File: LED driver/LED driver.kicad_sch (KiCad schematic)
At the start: 44 parts, among them J1 Conn_VCC, J2 Conn_LED, J3 Conn_UART, J4 Conn_Boot_Mode, J5 Conn_Aux, Q1 IRFZ44NS, Q2 IRFZ44NS, Q3 IRFZ44NS, Q4 IRFZ44NS, Q5 IRFZ44NS, SW1 SW_Push, U1 ESP32-C3-WROOM-02, U2 MP2359

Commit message: mostly finish led driver
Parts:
- added J1: Conn_VCC_ALT, TerminalBlock_Phoenix:TerminalBlock_Phoenix_MKDS-1,5-2_1x02_P5.00mm_Horizontal, symbol Connector_Generic:Conn_01x02
- D2: footprint Diode_SMD:D_SMB -> Diode_SMD:D_SMA
- J3: renamed from J1; footprint TerminalBlock_Phoenix:TerminalBlock_Phoenix_MKDS-1,5-2_1x02_P5.00mm_Horizontal -> Connector_BarrelJack:BarrelJack_CUI_PJ-063AH_Horizontal
- J6: renamed from J5; now not fitted
- L1: footprint Inductor_SMD:L_Bourns_SRP7028A_7.3x6.6mm -> Inductor_SMD:L_1210_3225Metric_Pad1.42x2.65mm_HandSolder
- Q1, Q2, Q3, Q4, Q5: footprint Package_TO_SOT_SMD:TO-263-2 -> Package_TO_SOT_SMD:SOT-23-3
- SW1: footprint Button_Switch_SMD:SW_Push_1P1T_NO_6x6mm_H9.5mm -> Button_Switch_SMD:SW_SPST_B3U-1000P
- renumbered C5 to C2, C2 to C4, C4 to C5, J3 to J5, R12 to R11, R22 to R12, R11 to R15, R15 to R17, R17 to R18, R18 to R19, R21 to R20
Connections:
- net GND: now also J1.1 (Pin_1)
- net PWM_B: now also R17.2
- net at F1.2, J3.2 (Pin_2): now also J1.2 (Pin_2)
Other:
- moved on the sheet: J3, R17

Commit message: led driver
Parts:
- C1: value .1uF -> 0.1uF
- Q1, Q2, Q3, Q4, Q5: value IRFZ44NS -> ZXMN3A01F; footprint Package_TO_SOT_SMD:SOT-23-3 -> Package_TO_SOT_SMD:SOT-23; symbol Custom:IRFZ44NS -> Transistor_FET:ZXMN3A01F
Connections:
- net B: now also Q2.3 (D); no longer Q2.2 (D)
- net G: now also Q4.3 (D); no longer Q4.2 (D)
- net GND: now also Q1.2 (S), Q2.2 (S), Q3.2 (S), Q4.2 (S), Q5.2 (S); no longer Q1.3 (S), Q2.3 (S), Q3.3 (S), Q4.3 (S), Q5.3 (S)
- net R: now also Q3.3 (D); no longer Q3.2 (D)
- net W: now also Q1.3 (D); no longer Q1.2 (D)
- net WW: now also Q5.3 (D); no longer Q5.2 (D)

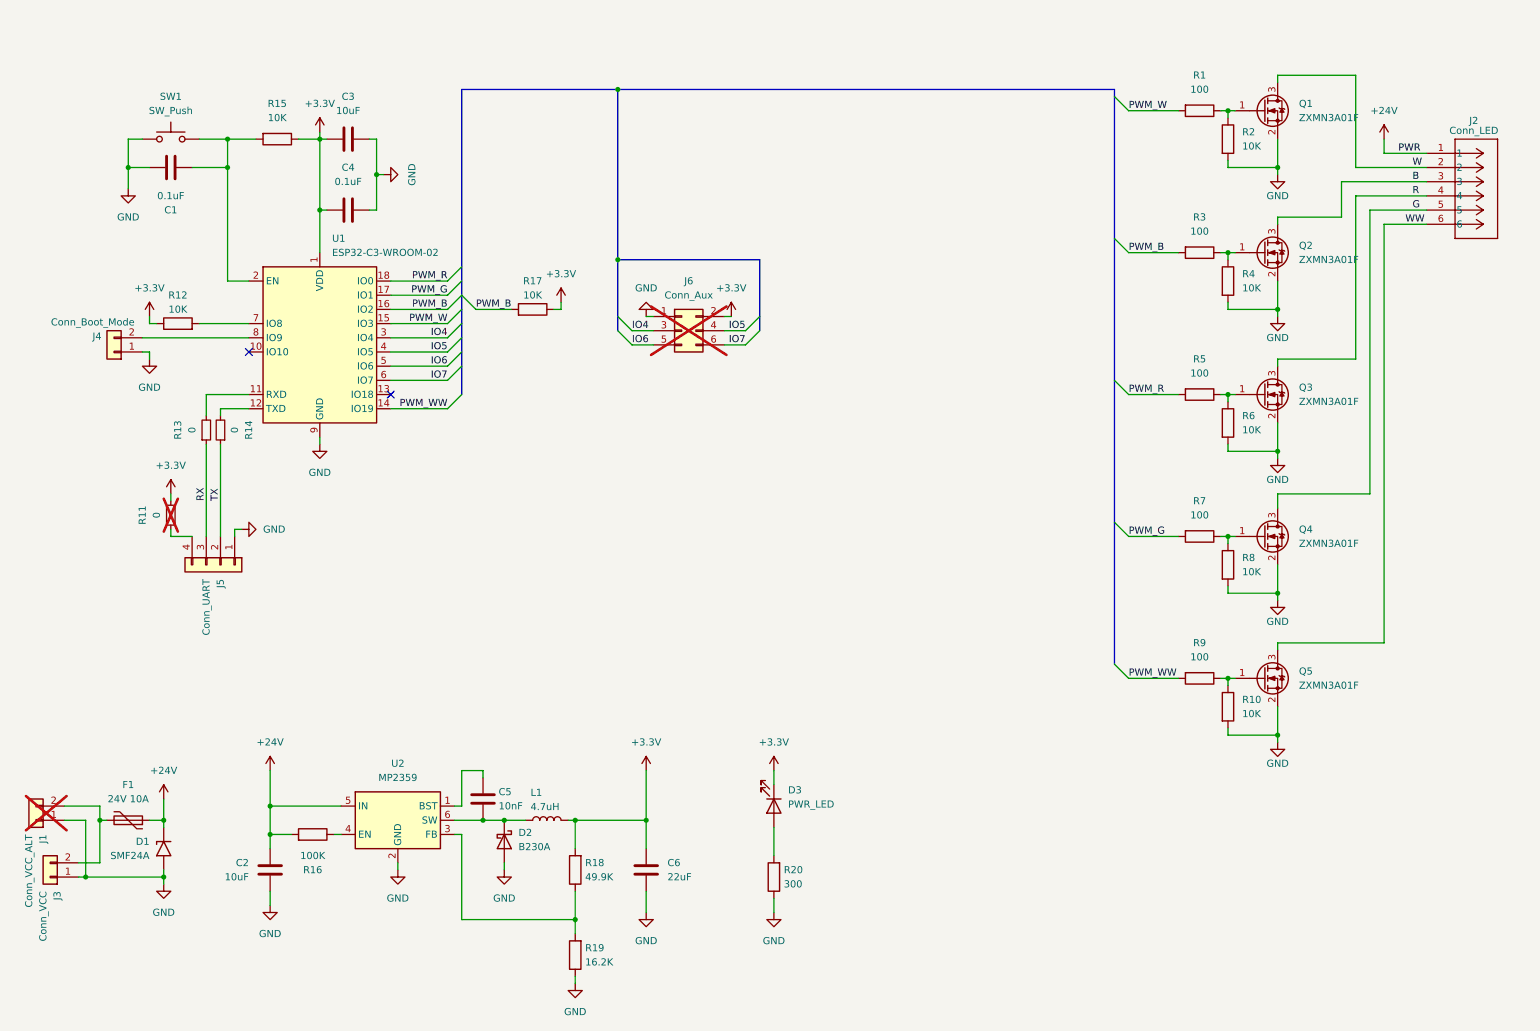
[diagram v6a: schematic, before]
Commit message: led driver parts
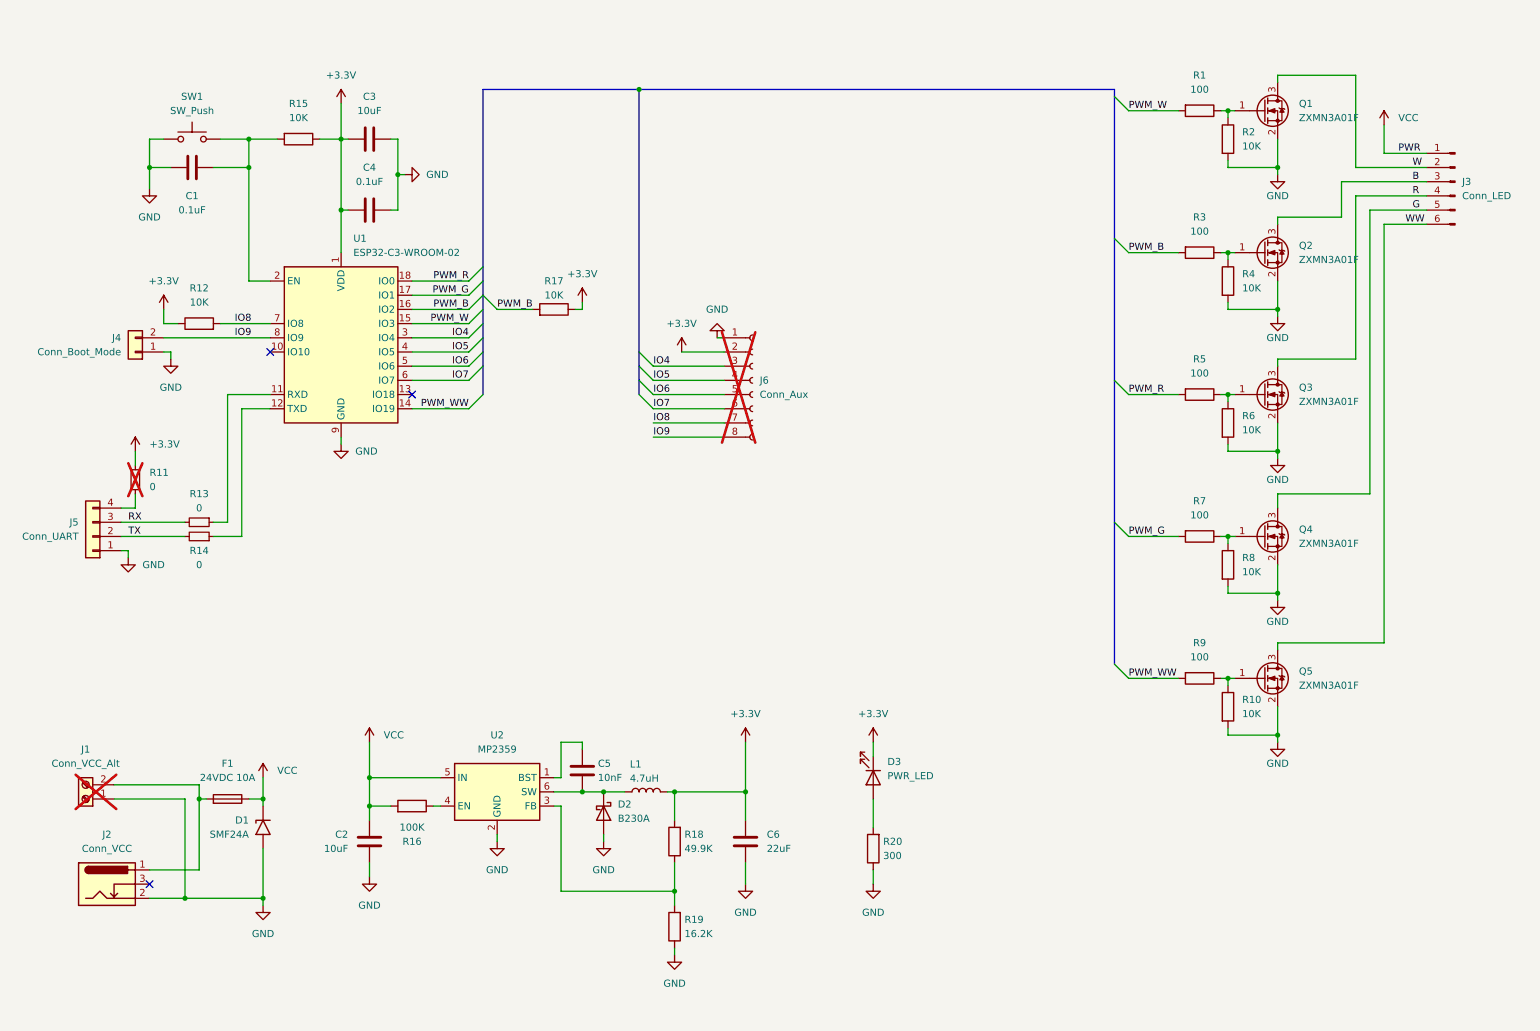
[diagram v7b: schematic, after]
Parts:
- F1: value 24V 10A -> 24VDC 10A; footprint Fuse:Fuse_1812_4532Metric_Pad1.30x3.40mm_HandSolder -> Fuse:Fuse_1206_3216Metric_Pad1.42x1.75mm_HandSolder; symbol Device:Polyfuse -> Device:Fuse
- J1: value Conn_VCC_ALT -> Conn_VCC_Alt; symbol Connector_Generic:Conn_01x02 -> Connector:Screw_Terminal_01x02
- J2: renamed from J3; footprint Connector_BarrelJack:BarrelJack_CUI_PJ-063AH_Horizontal -> Connector_BarrelJack:BarrelJack_GCT_DCJ200-10-A_Horizontal; symbol Connector_Generic:Conn_01x02 -> Connector:Barrel_Jack_Switch
- J3: renamed from J2; symbol 2024-04-03_06-42-17:532540670 -> Connector:Conn_01x06_Pin
- J6: footprint Connector_PinSocket_2.54mm:PinSocket_2x03_P2.54mm_Vertical -> Connector_PinSocket_2.54mm:PinSocket_2x04_P2.54mm_Vertical; symbol Connector_Generic:Conn_02x03_Odd_Even -> Connector:Conn_01x08_Socket
- renumbered R14 to R13, R13 to R14
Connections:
- net GND: now also J2.2; no longer J2.1 (Pin_1)
- net RX: now also R13.2; no longer R14.1
- net TX: now also R14.2; no longer R13.1
- net at U1.11 (RXD): now also R13.1; no longer R14.2
- net at U1.12 (TXD): now also R14.1; no longer R13.2
- net IO8: now reaches R12.2, U1.7 (IO8)
- net IO8: now also J6.7 (Pin_7)
- net IO9: now reaches J4.2 (Pin_2), U1.8 (IO9)
- net IO9: now also J6.8 (Pin_8)
- net at F1.2, J1.2 (Pin_2): now also J2.1; no longer J2.2 (Pin_2)
- net +24V renamed VCC
- no-connect marks 2 -> 3
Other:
- moved on the sheet: C1, C2, C3, C4, C5, C6, D1, D2, D3, J4, J5, L1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

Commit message: 2024-04-11
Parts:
- JP1: renamed from J4; value Conn_Boot_Mode -> Boot_Mode; footprint Connector_PinHeader_2.54mm:PinHeader_1x02_P2.54mm_Vertical -> Connector_PinHeader_2.00mm:PinHeader_1x02_P2.00mm_Vertical; symbol Connector_Generic:Conn_01x02 -> Jumper:Jumper_2_Open
- JP2: renamed from R11; value 0 -> SolderJumper_2_Open; footprint Resistor_SMD:R_0603_1608Metric_Pad0.98x0.95mm_HandSolder -> Jumper:SolderJumper-2_P1.3mm_Open_RoundedPad1.0x1.5mm; symbol Device:R_Small -> Jumper:SolderJumper_2_Open; now fitted; now left out of the parts list
- renumbered C3 to C1, C1 to C2, C4 to C3, C5 to C4, C2 to C5, D3 to D1, D1 to D3, J6 to J1, J5 to J2, J1 to J4, J2 to J5, R15 to R11, R17 to R12, R12 to R13, R13 to R14, R14 to R15, R18 to R17, R20 to R18
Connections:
- net +3.3V: now also JP2.1 (A); no longer JP2.2
- net GND: now also JP1.2 (B); no longer JP1.1 (Pin_1)
- net IO9: now also JP1.1 (A); no longer JP1.2 (Pin_2)
- net at J2.4 (Pin_4): now also JP2.2 (B); no longer JP2.1
